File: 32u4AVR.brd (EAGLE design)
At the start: 63.5 x 71.1 mm, 34 parts, among them IC1 MCP1252-33X50

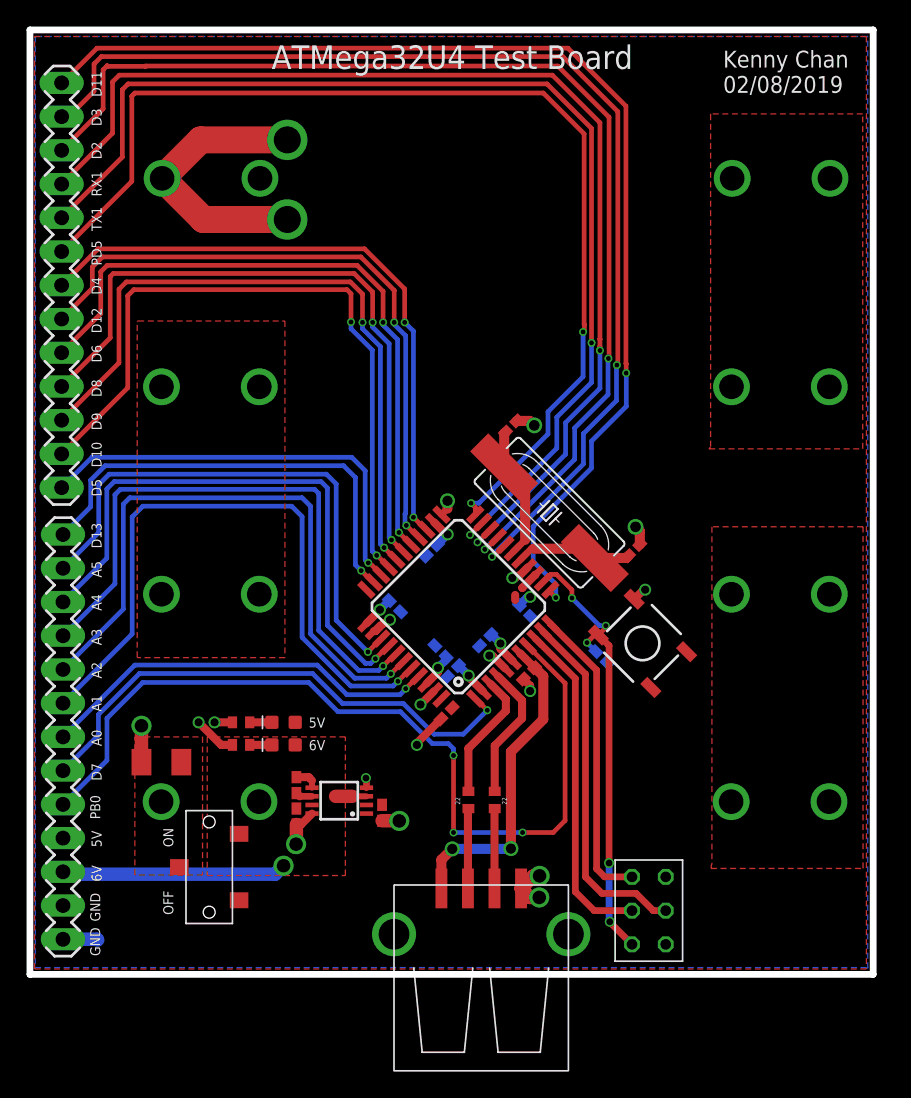
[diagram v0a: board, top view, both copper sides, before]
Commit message: Replaced USB A with micro USB
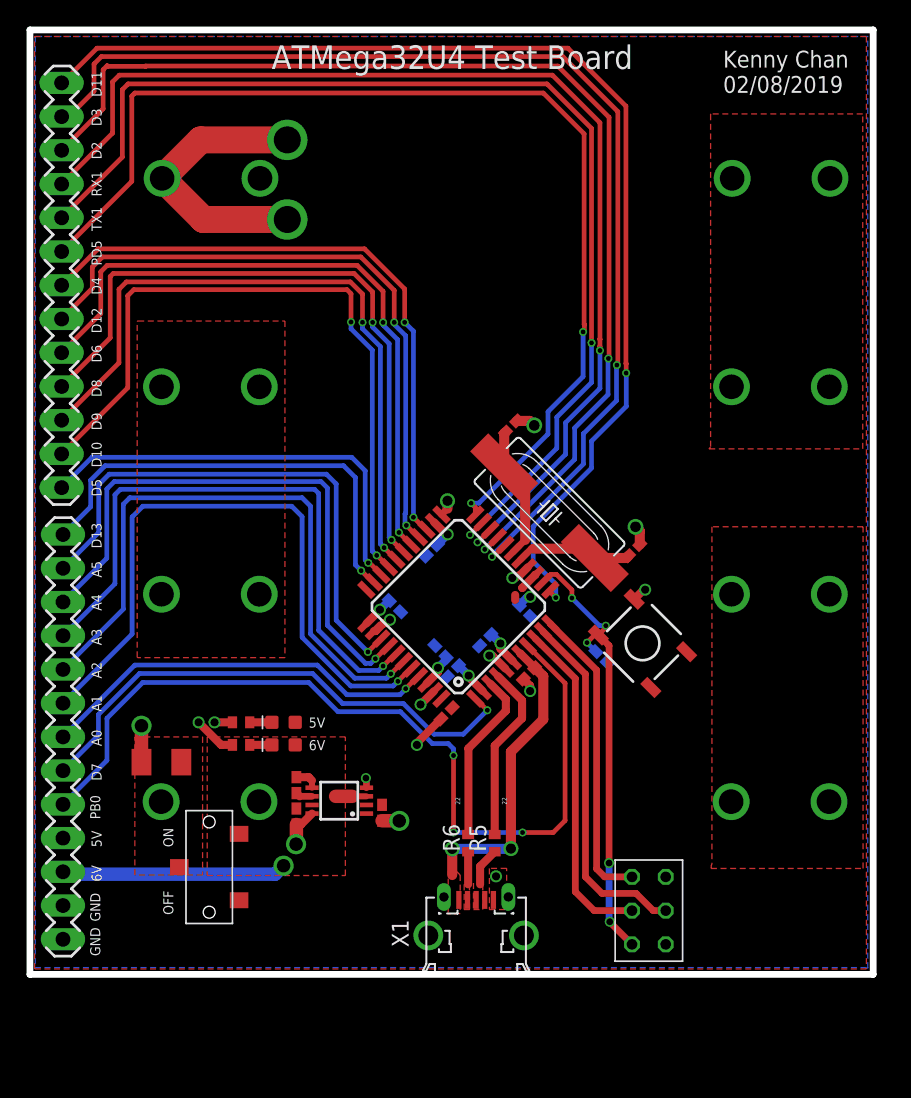
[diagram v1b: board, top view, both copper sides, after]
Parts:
- removed R1, R2: 22, resistor:R0402
- added R5, R6: 22, resistor:R0402
- X1: value (none) -> ZX62D-B-5PA8; device con-usb-3:USB-A-S -> zx62d-b-5pa8-oshpark_10:ZX62D-B-5PA8
- moved X1 2.28 mm to (46.3, -4.30)
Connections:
- net D+: now also R5.2; no longer R2.2
- net D-: now also R6.2; no longer R1.2
- net GND: now also X1.5; no longer X1.GND
- net N$6: now also R6.1, X1.2; no longer R1.1, X1.D-
- net N$7: now also R5.1, X1.3; no longer R2.1, X1.D+
- net VBUS: now also X1.1; no longer X1.VBUS
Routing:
- net GND: track 55.2 -> 48.9 mm, vias 20 -> 19
- net N$6: track 6.02 -> 2.45 mm
- net D-: track 9.76 -> 13.0 mm
- net D+: track 10.3 -> 13.5 mm
- net N$7: track 6.02 -> 2.91 mm
- net VBUS: track 24.2 -> 22.8 mm
- added copper zone on layer 1, net GND
- added copper zone on layer 1, net N$6
- added copper zone on layer 1, net N$7
- added copper zone on layer 1, net VBUS
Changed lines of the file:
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@@
 <attribute name="VALUE" x="17.8562" y="-3.7084" size="0.6096" layer="27" font="vector" ratio="20" rot="R90"/>
 </element>
-<element name="R1" library="resistor" library_urn="urn:adsk.eagle:library:348" package="R0402" package3d_urn="urn:adsk.eagle:package:26058/1" value="22" x="45.72" y="8.0518" smashed="yes" rot="R90"/>
-<element name="R2" library="resistor" library_urn="urn:adsk.eagle:library:348" package="R0402" package3d_urn="urn:adsk.eagle:package:26058/1" value="22" x="47.7012" y="8.0518" smashed="yes" rot="R90"/>
 <element name="S1" library="AP_quad" package="TACTILE-SWITCH-SMD" value="SWITCH-MOMENTARY-2SMD" x="58.831625" y="19.84509375" smashed="yes" rot="R315">
 <attribute name="PROD_ID" value="SWCH-08247" x="20.216525" y="-67.2633875" size="1.778" layer="27" rot="R315" display="off"/>
@@
 </element>
 <element name="U$3" library="adafruit" library_urn="urn:adsk.eagle:library:420" package="TQFP44" package3d_urn="urn:adsk.eagle:package:6240644/1" value="ATMEGA32U4-AU" x="44.966109375" y="22.6110125" smashed="yes" rot="R135"/>
-<element name="X1" library="con-usb-3" package="USB-A-S" value="" x="46.6852" y="-2.0574" smashed="yes" rot="R90"/>
 <element name="Y1" library="AP_quad" package="HC49UP" value="" x="51.827025" y="29.68745625" smashed="yes" rot="R315">
 <attribute name="VALUE" x="44.822425" y="30.7650875" size="1.27" layer="27" ratio="10" rot="R315"/>
@@
 <element name="C15" library="resistor" library_urn="urn:adsk.eagle:library:348" package="C1206K" package3d_urn="urn:adsk.eagle:package:26202/1" value="100uF" x="22.6" y="10.9" smashed="yes" rot="R180">
 <attribute name="VALUE" x="23.5" y="12.3" size="0.3556" layer="27" rot="R180"/>
+</element>
+<element name="R5" library="resistor" library_urn="urn:adsk.eagle:library:348" package="R0402" package3d_urn="urn:adsk.eagle:package:26058/1" value="22" x="47.7" y="4.8" smashed="yes" rot="R90">
+<attribute name="NAME" x="47.065" y="4.165" size="1.27" layer="25" rot="R90"/>
+<attribute name="VALUE" x="49.605" y="4.165" size="1.27" layer="27" rot="R90"/>
+</element>
+<element name="R6" library="resistor" library_urn="urn:adsk.eagle:library:348" package="R0402" package3d_urn="urn:adsk.eagle:package:26058/1" value="22" x="45.7" y="4.8" smashed="yes" rot="R90">
+<attribute name="NAME" x="45.065" y="4.165" size="1.27" layer="25" rot="R90"/>
+<attribute name="VALUE" x="47.605" y="4.165" size="1.27" layer="27" rot="R90"/>
+</element>
+<element name="X1" library="zx62d-b-5pa8-oshpark_10" package="ZX62D-B-5PA8" value="ZX62D-B-5PA8" x="46.3" y="-4.3" smashed="yes" rot="R90">
+<attribute name="MF" value="Hirose" x="46.3" y="-4.3" size="1.778" layer="27" rot="R90" display="off"/>
+<attribute name="MPN" value="ZX62D-B-5PA8" x="46.3" y="-4.3" size="1.778" layer="27" rot="R90" display="off"/>
+<attribute name="NAME" x="41.22" y="-3.03" size="1.27" layer="25" rot="R90"/>
+<attribute name="OC_FARNELL" value="2300438" x="46.3" y="-4.3" size="1.778" layer="27" rot="R90" display="off"/>
+<attribute name="OC_NEWARK" value="69W0712" x="46.3" y="-4.3" size="1.778" layer="27" rot="R90" display="off"/>
+<attribute name="VALUE" x="52.65" y="-3.03" size="1.27" layer="27" rot="R90"/>
 </element>
 </elements>
@@
 <contactref element="C2" pad="1"/>
 <contactref element="BT1" pad="GND@1"/>
-<contactref element="X1" pad="GND"/>
 <contactref element="U$1" pad="GND"/>
 <contactref element="C4" pad="2"/>
@@
 <wire x1="58.627271875" y1="28.29770625" x2="58.303984375" y2="28.620996875" width="0.762" layer="1"/>
 <via x="58.303984375" y="28.620996875" extent="1-16" drill="0.8"/>
-<wire x1="58.303984375" y1="28.620996875" x2="58.149125" y2="28.466140625" width="0.762" layer="16"/>
 <wire x1="49.359646875" y1="36.5954625" x2="50.343090625" y2="36.595465625" width="0.762" layer="1"/>
 <wire x1="50.343090625" y1="36.595465625" x2="50.677553125" y2="36.261003125" width="0.762" layer="1"/>
@@
 <wire x1="49.2407125" y1="24.766275" x2="49.0251875" y2="24.766275" width="0.6096" layer="1"/>
 <via x="59.029190625" y="23.886209375" extent="1-16" drill="0.6096"/>
-<wire x1="49.6852" y1="1.3926" x2="50.3666" y2="0.7112" width="1.016" layer="1"/>
-<wire x1="50.3666" y1="0.7112" x2="51.054" y2="0.7112" width="1.016" layer="1"/>
-<via x="51.054" y="0.7112" extent="1-16" drill="1.016"/>
-<wire x1="49.6852" y1="1.3926" x2="50.6294" y2="2.3368" width="1.016" layer="1"/>
-<wire x1="50.6294" y1="2.3368" x2="51.0794" y2="2.3368" width="1.016" layer="1"/>
-<via x="51.0794" y="2.3368" extent="1-16" drill="1.016"/>
 <wire x1="39.2176" y1="6.4866" x2="40.5034" y2="6.4866" width="1.016" layer="1"/>
 <wire x1="40.5034" y1="6.4866" x2="40.513" y2="6.477" width="1.016" layer="1"/>
@@
 <wire x1="33.9418" y1="7.026" x2="33.123" y2="6.2072" width="0.6096" layer="1"/>
 <wire x1="33.123" y1="6.2072" x2="32.766" y2="6.2072" width="0.6096" layer="1"/>
-<wire x1="15.1892" y1="-2.4384" x2="17.7546" y2="-2.4384" width="1.016" layer="16"/>
-<wire x1="17.7546" y1="-2.4384" x2="17.8054" y2="-2.4892" width="1.016" layer="16"/>
 <wire x1="43.65215625" y1="14.148784375" x2="41.8402" y2="12.336828125" width="0.6096" layer="1"/>
 <wire x1="41.8402" y1="12.336828125" x2="41.8402" y2="12.2" width="0.6096" layer="1"/>
@@
 <wire x1="21.1" y1="10.9" x2="21.1" y2="13.6398" width="1.016" layer="1"/>
 <via x="21.1" y="13.6398" extent="1-16" drill="1.016"/>
+<contactref element="X1" pad="5"/>
+<polygon width="0.1016" layer="1" thermals="no">
+<vertex x="47.3" y="2.9"/>
+<vertex x="47.3" y="-0.2"/>
+<vertex x="48.6" y="-0.2"/>
+<vertex x="48.6" y="2.9"/>
+</polygon>
+<via x="47.8" y="2.3" extent="1-16" drill="0.6096"/>
 </signal>
 <signal name="N$3">
@@
 </signal>
 <signal name="VBUS">
-<contactref element="X1" pad="VBUS"/>
 <contactref element="C7" pad="1"/>
 <contactref element="U$3" pad="7"/>
-<wire x1="43.6852" y1="1.3926" x2="43.6852" y2="3.5532" width="0.762" layer="1"/>
-<wire x1="43.6852" y1="3.5532" x2="44.5008" y2="4.3688" width="0.762" layer="1"/>
 <via x="44.5008" y="4.3688" extent="1-16" drill="0.762"/>
 <wire x1="44.5008" y1="4.3688" x2="48.895" y2="4.3688" width="0.762" layer="16"/>
@@
 <wire x1="50.72294375" y1="18.00945625" x2="50.7072" y2="18.00945625" width="0.762" layer="1"/>
 <wire x1="48.9204" y1="11.684" x2="51.3588" y2="14.1224" width="0.762" layer="1"/>
-</signal>
-<signal name="N$6">
-<contactref element="X1" pad="D-"/>
-<contactref element="R1" pad="1"/>
-<wire x1="45.6852" y1="1.3926" x2="45.6852" y2="7.367" width="0.6096" layer="1"/>
-<wire x1="45.6852" y1="7.367" x2="45.72" y2="7.4018" width="0.6096" layer="1"/>
-</signal>
-<signal name="N$7">
-<contactref element="R2" pad="1"/>
-<contactref element="X1" pad="D+"/>
-<wire x1="47.6852" y1="1.3926" x2="47.6852" y2="7.3858" width="0.6096" layer="1"/>
-<wire x1="47.6852" y1="7.3858" x2="47.7012" y2="7.4018" width="0.6096" layer="1"/>
+<wire x1="44.5008" y1="2.3992" x2="44.5008" y2="4.3688" width="0.762" layer="1"/>
+<contactref element="X1" pad="1"/>
+<polygon width="0.1016" layer="1" thermals="no">
+<vertex x="44.2" y="2.68"/>
+<vertex x="44.82" y="2.68"/>
+<vertex x="45.1" y="2.4"/>
+<vertex x="45.1" y="-0.5"/>
+<vertex x="44.2" y="-0.5"/>
+</polygon>
 </signal>
 <signal name="D-">
-<contactref element="R1" pad="2"/>
 <contactref element="U$3" pad="3"/>
-<wire x1="45.72" y1="8.7018" x2="45.72" y2="11.938" width="0.6096" layer="1"/>
-<wire x1="45.72" y1="11.938" x2="48.5394" y2="14.7574" width="0.6096" layer="1"/>
+<wire x1="48.5394" y1="14.7574" x2="45.72" y2="11.938" width="0.6096" layer="1"/>
 <wire x1="48.5394" y1="14.7574" x2="48.5394" y2="15.64360625" width="0.6096" layer="1"/>
 <wire x1="48.5394" y1="15.64360625" x2="47.370271875" y2="16.812734375" width="0.6096" layer="1"/>
+<contactref element="R6" pad="2"/>
+<wire x1="45.72" y1="11.938" x2="45.72" y2="5.47" width="0.6096" layer="1"/>
+<wire x1="45.72" y1="5.47" x2="45.7" y2="5.45" width="0.6096" layer="1"/>
 </signal>
 <signal name="D+">
-<contactref element="R2" pad="2"/>
 <contactref element="U$3" pad="4"/>
-<wire x1="47.7012" y1="8.7018" x2="47.7012" y2="12.1412" width="0.6096" layer="1"/>
-<wire x1="47.7012" y1="12.1412" x2="49.7586" y2="14.1986" width="0.6096" layer="1"/>
+<wire x1="49.7586" y1="14.1986" x2="47.7012" y2="12.1412" width="0.6096" layer="1"/>
 <wire x1="49.7586" y1="14.1986" x2="49.7586" y2="15.555778125" width="0.6096" layer="1"/>
 <wire x1="49.7586" y1="15.555778125" x2="47.93595625" y2="17.378421875" width="0.6096" layer="1"/>
+<contactref element="R5" pad="2"/>
+<wire x1="47.7012" y1="12.1412" x2="47.7012" y2="5.4512" width="0.6096" layer="1"/>
+<wire x1="47.7012" y1="5.4512" x2="47.7" y2="5.45" width="0.6096" layer="1"/>
 </signal>
 <signal name="MOSI">
@@
 <wire x1="29.25" y1="12.2" x2="30.923" y2="12.2" width="0.6096" layer="1"/>
 </signal>
+<signal name="N$6">
+<contactref element="X1" pad="2"/>
+<contactref element="R6" pad="1"/>
+<wire x1="45.7" y1="4.15" x2="45.7" y2="1.7" width="0.6096" layer="1"/>
+<polygon width="0.1016" layer="1" thermals="no">
+<vertex x="45.4" y="1.7"/>
+<vertex x="45.8" y="1.7"/>
+<vertex x="45.8" y="-0.2"/>
+<vertex x="45.4" y="-0.2"/>
+</polygon>
+</signal>
+<signal name="N$7">
+<contactref element="R5" pad="1"/>
+<contactref element="X1" pad="3"/>
+<wire x1="47.7" y1="4.15" x2="46.6" y2="3.05" width="0.6096" layer="1"/>
+<wire x1="46.6" y1="3.05" x2="46.6" y2="1.7" width="0.6096" layer="1"/>
+<polygon width="0.1016" layer="1" thermals="no">
+<vertex x="46.1" y="1.8"/>
+<vertex x="46.1" y="-0.2"/>
+<vertex x="46.8" y="-0.2"/>
+<vertex x="46.8" y="1.8"/>
+</polygon>
+</signal>
 </signals>
